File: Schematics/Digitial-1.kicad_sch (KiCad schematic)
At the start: 8 parts, among them J19 To Compute #1, J20 Conn_01x04, J21 Conn_01x04, J22 Conn_01x02, J23 To Compute #1, U17 ESP32-DEVKIT-V1, U18 USB Host Shield 2.0

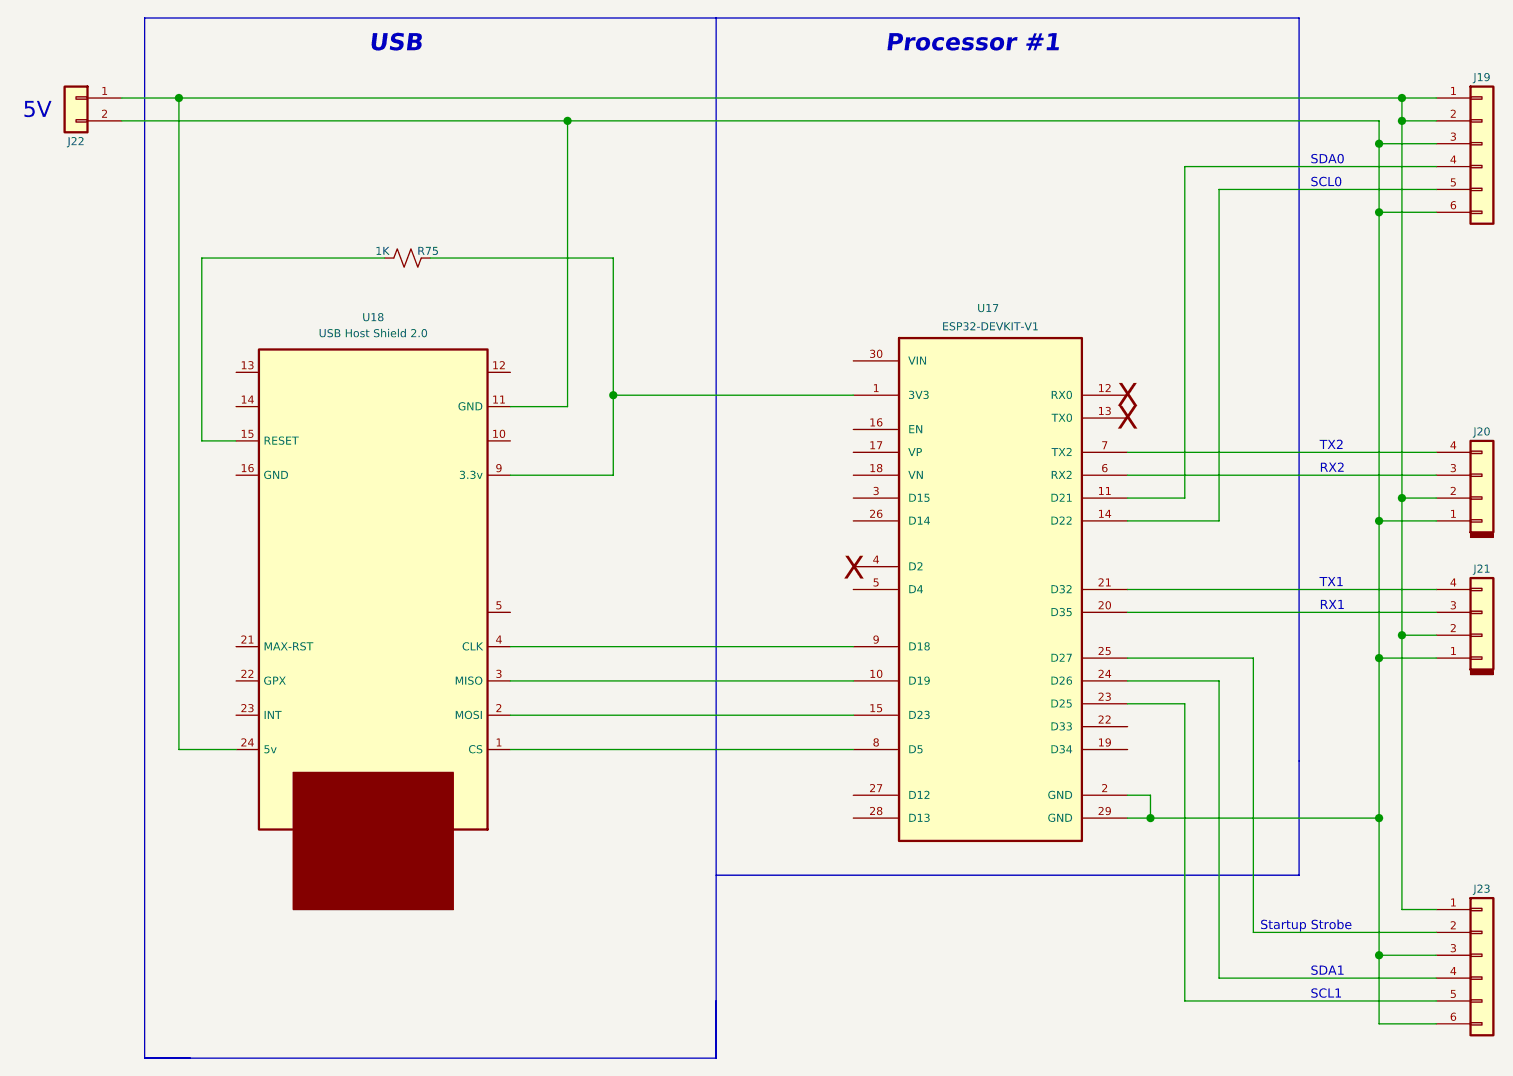
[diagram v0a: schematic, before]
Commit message: Upgreade byte value interface to short.  First stage of refactoring midi input for rotory encoders.  Still needs scaling.
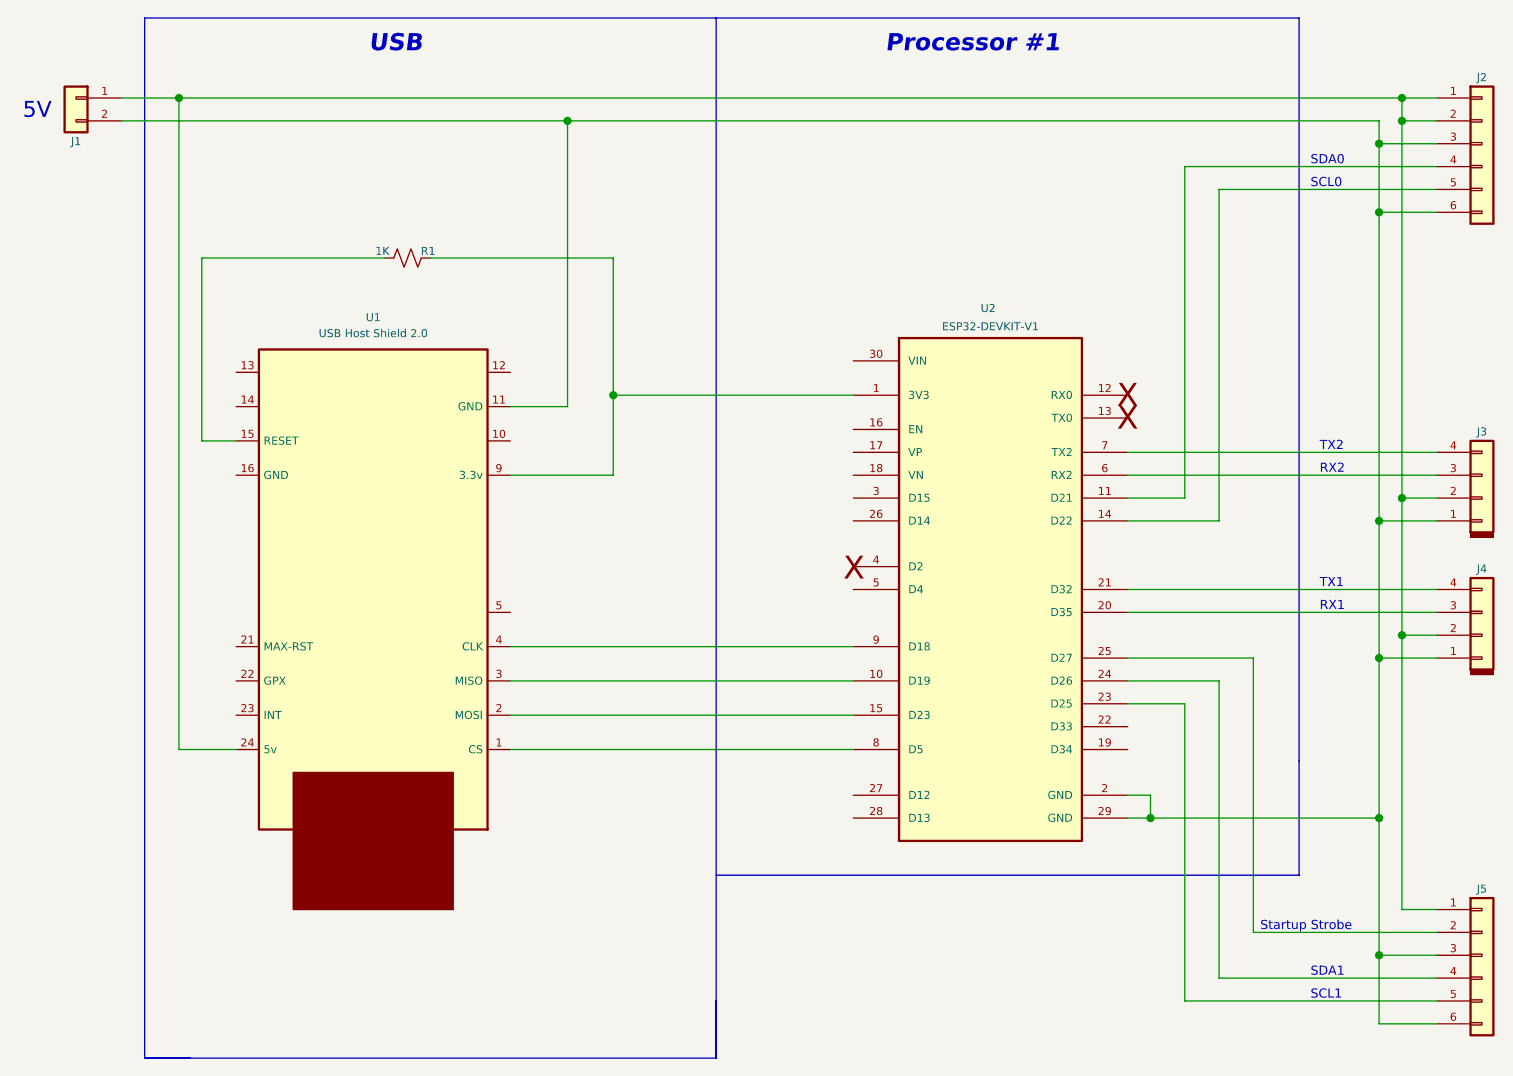
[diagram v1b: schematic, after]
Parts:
- renumbered J22 to J1, J19 to J2, J20 to J3, J21 to J4, J23 to J5, R75 to R1, U18 to U1, U17 to U2
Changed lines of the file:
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@@
 		(on_board yes)
 		(dnp no)
-		(property "Reference" "U17"
+		(property "Reference" "U2"
 			(at 188.976 69.088 0)
 			(effects
@@
 			(project "Schematics-Midi32"
 				(path "/718f017d-28fe-4e29-b548-40db8e21cec7/5f23d779-3412-4b06-96f4-480c60744fb9"
-					(reference "U17")
+					(reference "U2")
 					(unit 1)
 				)
@@
 		(on_board yes)
 		(dnp no)
-		(property "Reference" "J19"
+		(property "Reference" "J2"
 			(at 243.84 43.434 0)
 			(effects
@@
 			(project "Schematics-Midi32"
 				(path "/718f017d-28fe-4e29-b548-40db8e21cec7/5f23d779-3412-4b06-96f4-480c60744fb9"
-					(reference "J19")
+					(reference "J2")
 					(unit 1)
 				)
@@
 		(on_board yes)
 		(dnp no)
-		(property "Reference" "J22"
+		(property "Reference" "J1"
 			(at 87.63 50.546 0)
 			(effects
@@
 			(project "Schematics-Midi32"
 				(path "/718f017d-28fe-4e29-b548-40db8e21cec7/5f23d779-3412-4b06-96f4-480c60744fb9"
-					(reference "J22")
+					(reference "J1")
 					(unit 1)
 				)
@@
 		(on_board yes)
 		(dnp no)
-		(property "Reference" "J23"
+		(property "Reference" "J5"
 			(at 243.84 133.604 0)
 			(effects
@@
 			(project "Schematics-Midi32"
 				(path "/718f017d-28fe-4e29-b548-40db8e21cec7/5f23d779-3412-4b06-96f4-480c60744fb9"
-					(reference "J23")
+					(reference "J5")
 					(unit 1)
 				)
@@
 		(on_board yes)
 		(dnp no)
-		(property "Reference" "J21"
+		(property "Reference" "J4"
 			(at 243.84 98.044 0)
 			(effects
@@
 			(project "Schematics-Midi32"
 				(path "/718f017d-28fe-4e29-b548-40db8e21cec7/5f23d779-3412-4b06-96f4-480c60744fb9"
-					(reference "J21")
+					(reference "J4")
 					(unit 1)
 				)
@@
 		(on_board yes)
 		(dnp no)
-		(property "Reference" "U18"
+		(property "Reference" "U1"
 			(at 120.65 70.104 0)
 			(effects
@@
 			(project "Schematics-Midi32"
 				(path "/718f017d-28fe-4e29-b548-40db8e21cec7/5f23d779-3412-4b06-96f4-480c60744fb9"
-					(reference "U18")
+					(reference "U1")
 					(unit 1)
 				)
@@
 		(on_board yes)
 		(dnp no)
-		(property "Reference" "R75"
+		(property "Reference" "R1"
 			(at 126.746 62.738 90)
 			(effects
@@
 			(project "Schematics-Midi32"
 				(path "/718f017d-28fe-4e29-b548-40db8e21cec7/5f23d779-3412-4b06-96f4-480c60744fb9"
-					(reference "R75")
+					(reference "R1")
 					(unit 1)
 				)
@@
 		(on_board yes)
 		(dnp no)
-		(property "Reference" "J20"
+		(property "Reference" "J3"
 			(at 243.84 82.804 0)
 			(effects
@@
 			(project "Schematics-Midi32"
 				(path "/718f017d-28fe-4e29-b548-40db8e21cec7/5f23d779-3412-4b06-96f4-480c60744fb9"
-					(reference "J20")
-					(unit 1)
-				)
+					(reference "J3")
+					(unit 1)
+				)

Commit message: Updated schematics including VCO and VCF daughter boards
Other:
- company:       MLE Tech                  Cedar Park, TX -> (none)
- title: Synth #2 -> Processor Module
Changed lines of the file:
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@@
 	(paper "USLegal")
 	(title_block
-		(title "Synth #2")
-		(date "2023-07-27")
-		(rev "0.1")
-		(company "      MLE Tech                  Cedar Park, TX")
-		(comment 2 "In Development")
+		(title "Processor Module")
+		(date "2025-01-16")
+		(rev "2.6")
+		(comment 1 "In Development ")
 	)
 	(junction
